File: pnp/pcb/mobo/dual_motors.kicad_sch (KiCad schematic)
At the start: 18 parts, among them J30 TMC_PIN_HEADER, M5 MOTOR1, M6 MOTOR2

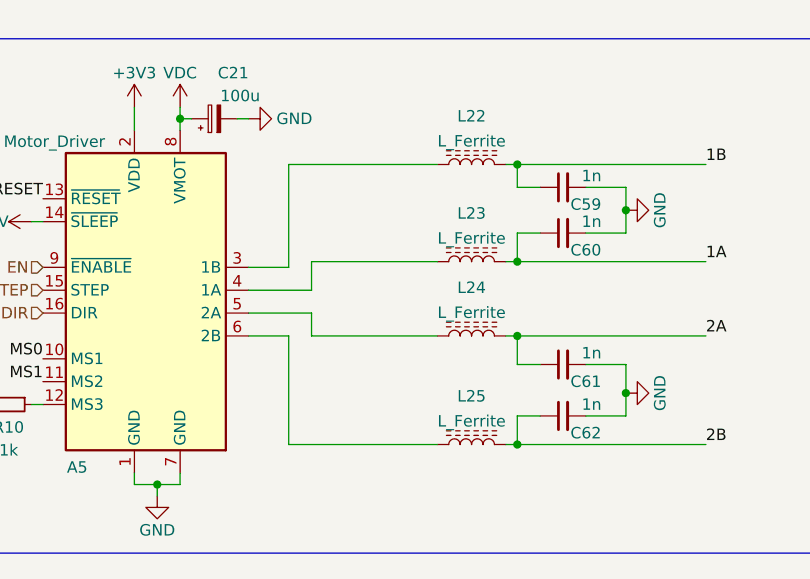
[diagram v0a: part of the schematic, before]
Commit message: tweak PN of mobo
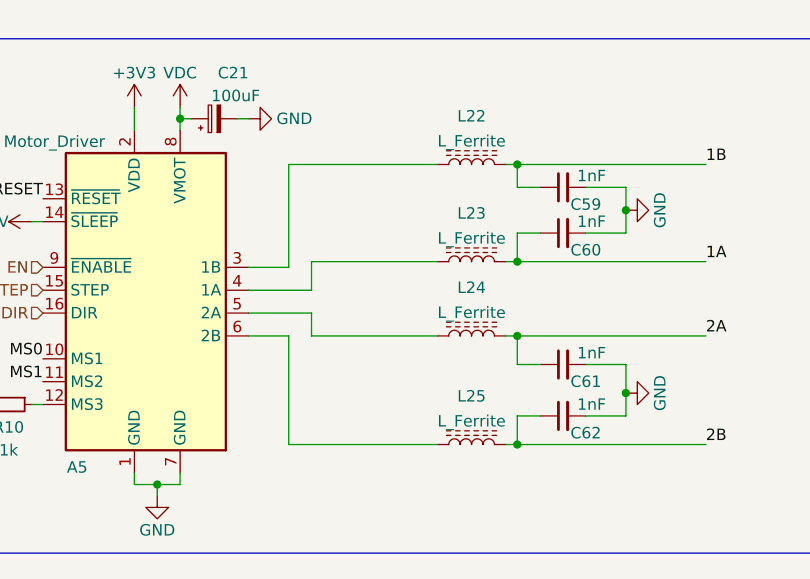
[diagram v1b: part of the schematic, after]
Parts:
- A5: LCSC (none) -> C27438 x2
- C21: value 100u -> 100uF
- C59, C60, C61, C62: value 1n -> 1nF; LCSC (none) -> C94121
- J30: LCSC (none) -> C49661
- JP17, JP18, JP19, JP20: LCSC (none) -> DNP
- L22, L23, L24, L25: LCSC (none) -> C79382
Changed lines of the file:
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@@
+      (effects (font (size 1.27 1.27)) hide)
+    )
+    (property "LCSC" "C27438 x2" (at 80.645 105.41 0)
       (effects (font (size 1.27 1.27)) hide)
     )
@@
       (effects (font (size 1.27 1.27)) (justify left))
     )
-    (property "Value" "100u" (at 94.615 83.82 90)
+    (property "Value" "100uF" (at 94.615 83.82 90)
       (effects (font (size 1.27 1.27)) (justify left))
     )
@@
       (effects (font (size 1.27 1.27)) hide)
     )
+    (property "LCSC" "DNP" (at 189.23 90.17 0)
+      (effects (font (size 1.27 1.27)) hide)
+    )
     (pin "1")
     (pin "2")
@@
       (effects (font (size 1.27 1.27)) hide)
     )
+    (property "LCSC" "DNP" (at 215.9 90.17 0)
+      (effects (font (size 1.27 1.27)) hide)
+    )
     (pin "1")
     (pin "2")
@@
       (effects (font (size 1.27 1.27)) hide)
     )
+    (property "LCSC" "DNP" (at 189.23 111.76 0)
+      (effects (font (size 1.27 1.27)) hide)
+    )
     (pin "1")
     (pin "2")
@@
       (effects (font (size 1.27 1.27)))
     )
-    (property "Value" "1n" (at 131.445 92.71 90)
+    (property "Value" "1nF" (at 131.445 92.71 90)
       (effects (font (size 1.27 1.27)))
     )
@@
     )
     (property "Notes" "50V/10%" (at 128.27 93.98 0)
+      (effects (font (size 1.27 1.27)) hide)
+    )
+    (property "LCSC" "C94121" (at 128.27 93.98 0)
       (effects (font (size 1.27 1.27)) hide)
     )
@@
       (effects (font (size 1.27 1.27)) hide)
     )
+    (property "LCSC" "C79382" (at 118.11 122.555 0)
+      (effects (font (size 1.27 1.27)) hide)
+    )
     (pin "1")
     (pin "2")
@@
       (effects (font (size 1.27 1.27)) hide)
     )
+    (property "LCSC" "C49661" (at 194.31 135.89 0)
+      (effects (font (size 1.27 1.27)) hide)
+    )
     (pin "1")
     (pin "2")
@@
       (effects (font (size 1.27 1.27)))
     )
-    (property "Value" "1n" (at 131.445 112.395 90)
+    (property "Value" "1nF" (at 131.445 112.395 90)
       (effects (font (size 1.27 1.27)))
     )
@@
     )
     (property "Notes" "50V/10%" (at 128.27 113.665 0)
+      (effects (font (size 1.27 1.27)) hide)
+    )
+    (property "LCSC" "C94121" (at 128.27 113.665 0)
       (effects (font (size 1.27 1.27)) hide)
     )
@@
       (effects (font (size 1.27 1.27)) hide)
     )
+    (property "LCSC" "C79382" (at 118.11 102.235 0)
+      (effects (font (size 1.27 1.27)) hide)
+    )
     (pin "1")
     (pin "2")
@@
       (effects (font (size 1.27 1.27)) hide)
     )
+    (property "LCSC" "C79382" (at 118.11 91.44 0)
+      (effects (font (size 1.27 1.27)) hide)
+    )
     (pin "1")
     (pin "2")
@@
       (effects (font (size 1.27 1.27)) hide)
     )
+    (property "LCSC" "C79382" (at 118.11 110.49 0)
+      (effects (font (size 1.27 1.27)) hide)
+    )
     (pin "1")
     (pin "2")
@@
       (effects (font (size 1.27 1.27)))
     )
-    (property "Value" "1n" (at 131.445 118.11 90)
+    (property "Value" "1nF" (at 131.445 118.11 90)
       (effects (font (size 1.27 1.27)))
     )
@@
       (effects (font (size 1.27 1.27)) hide)
     )
+    (property "LCSC" "C94121" (at 128.27 119.38 0)
+      (effects (font (size 1.27 1.27)) hide)
+    )
     (pin "1")
     (pin "2")
@@
       (effects (font (size 1.27 1.27)))
     )
-    (property "Value" "1n" (at 131.445 97.79 90)
+    (property "Value" "1nF" (at 131.445 97.79 90)
       (effects (font (size 1.27 1.27)))
     )
@@
       (effects (font (size 1.27 1.27)) hide)
     )
+    (property "LCSC" "C94121" (at 128.27 99.06 0)
+      (effects (font (size 1.27 1.27)) hide)
+    )
     (pin "1")
     (pin "2")
@@
       (effects (font (size 1.27 1.27)) hide)
     )
+    (property "LCSC" "DNP" (at 215.9 111.76 0)
+      (effects (font (size 1.27 1.27)) hide)
+    )
